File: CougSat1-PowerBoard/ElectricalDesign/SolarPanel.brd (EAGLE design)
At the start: 80 x 97 mm, 110 parts, among them J1 Wire Harness Connector, U1 SPV1040, U2 SPV1040, U3 TCA9535R, U4 LTC2499, U5 LTC2499, U6 MCP1501-18

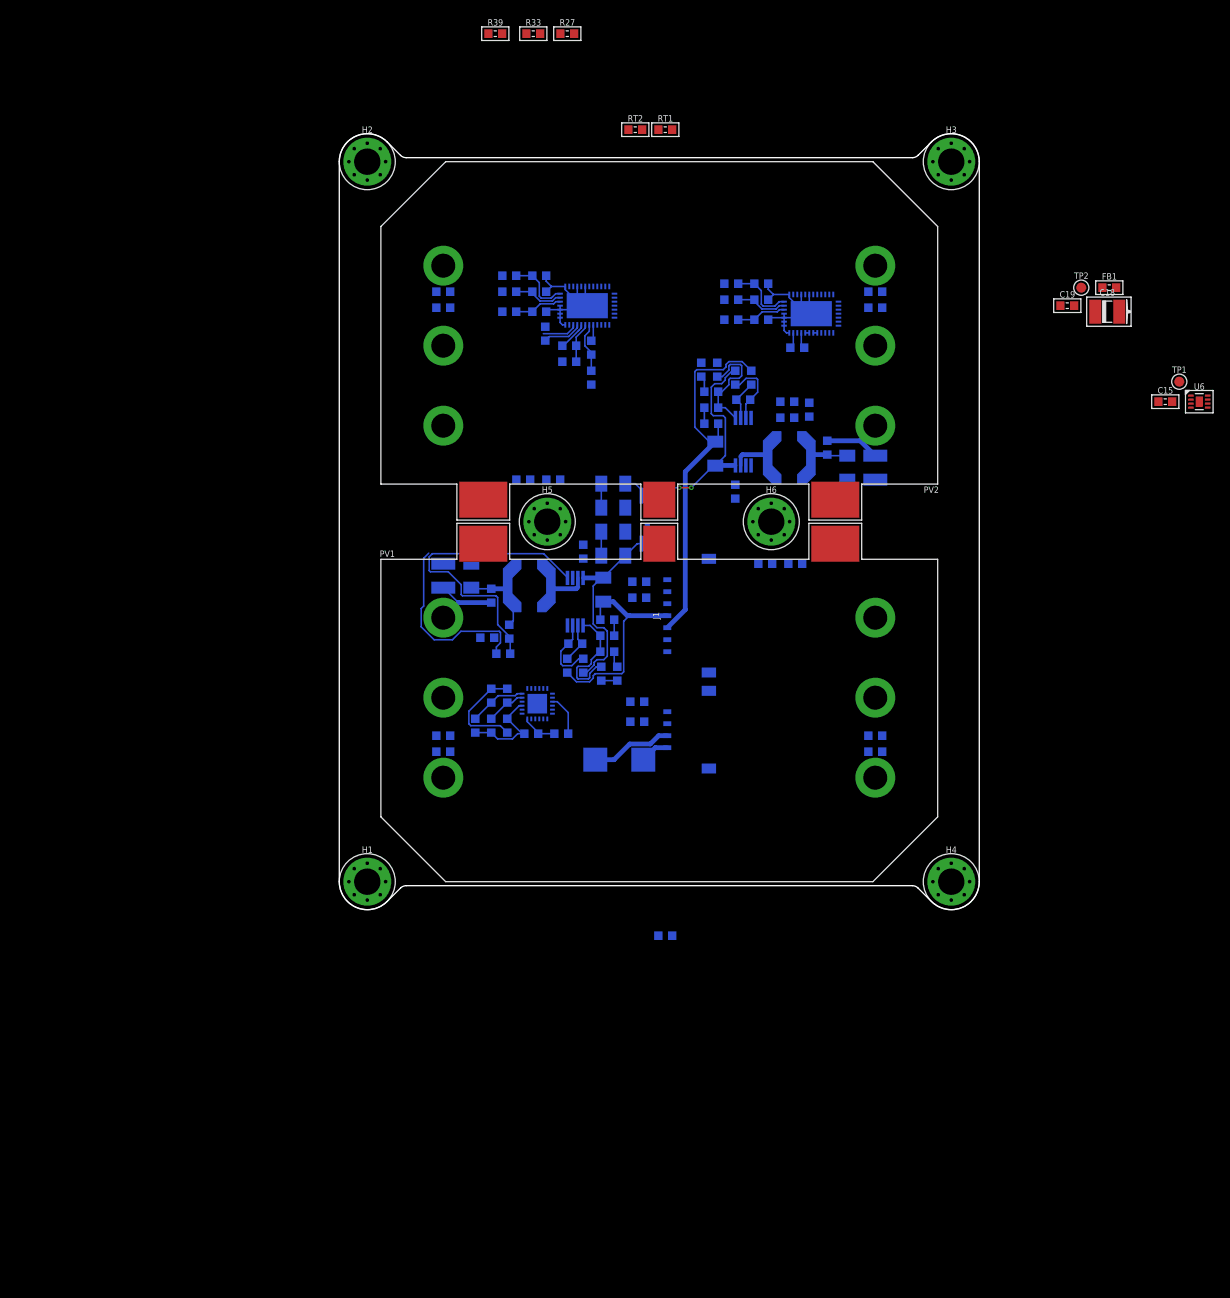
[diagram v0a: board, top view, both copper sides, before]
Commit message: Routed MPPTs, part of ADC
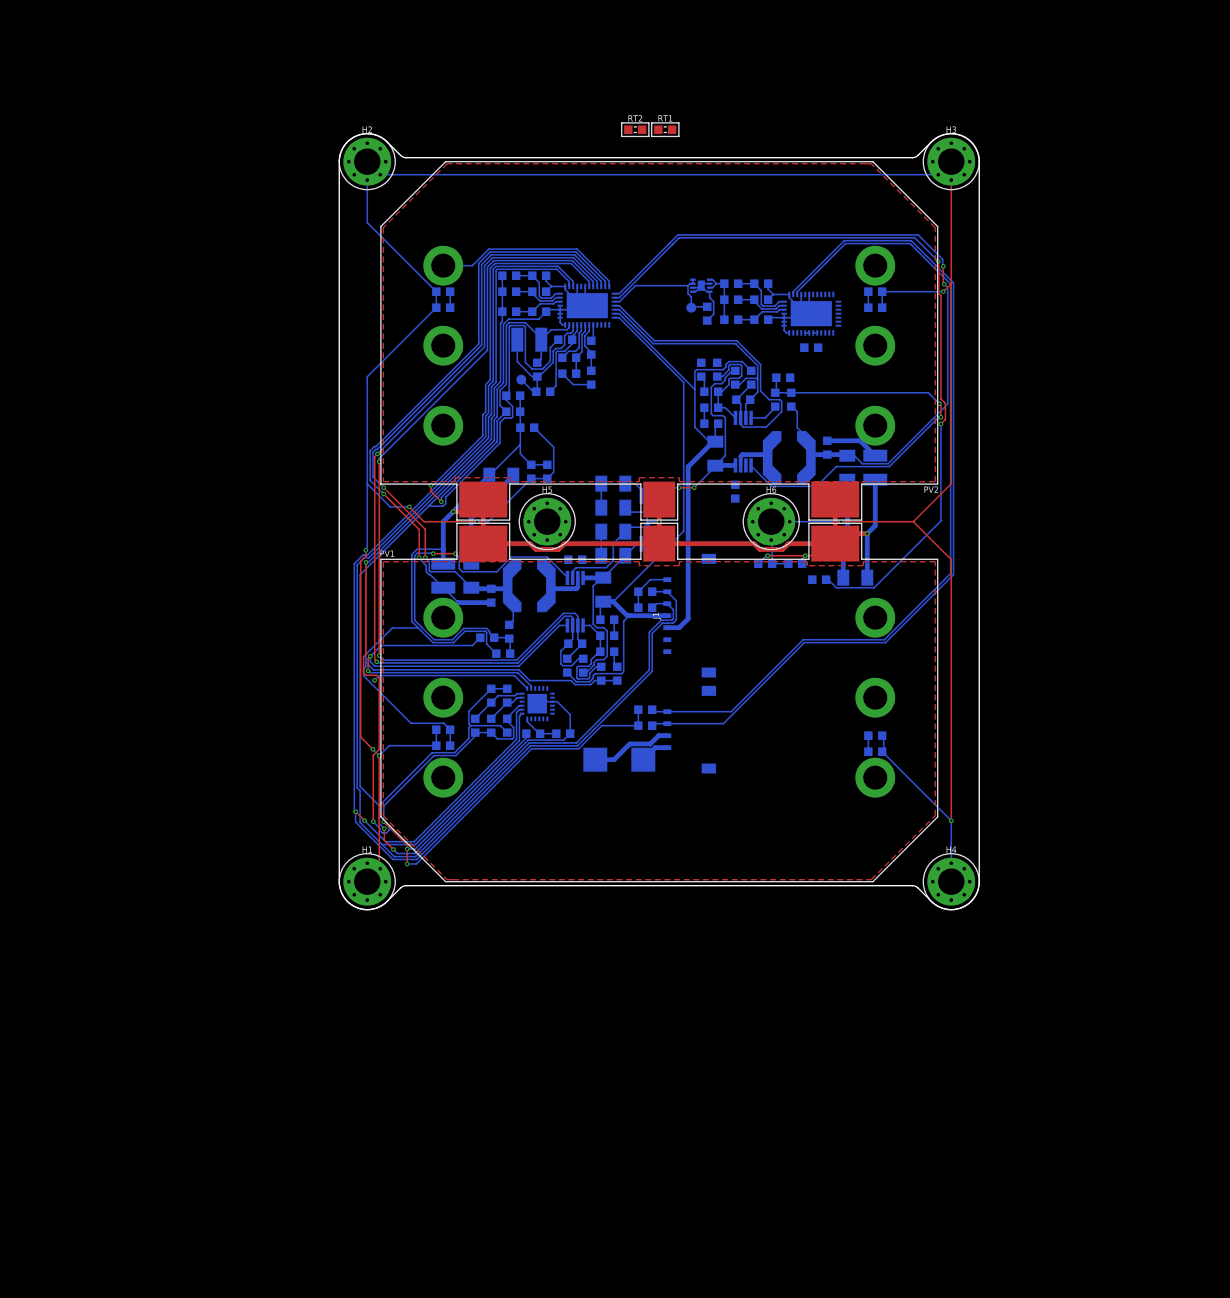
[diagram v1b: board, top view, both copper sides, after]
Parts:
- added C27, C28: 4.7µF 10%, CougsInSpace-Capacitors:3216
- moved C18 72.3 mm to (23.8, 72.2), flipped to the bottom
- moved FB1 71.9 mm to (25.5, 65.8), flipped to the bottom
- moved TP2 70.9 mm to (22.8, 67.2), flipped to the bottom
- moved C19 66.7 mm to (24.8, 68.5), flipped to the bottom, turned to 90 degrees
- moved U6 63.9 mm to (45.2, 79.0), flipped to the bottom
- moved TP1 61.7 mm to (44.0, 76.2), flipped to the bottom
- moved C15 58.3 mm to (46.0, 75.5), flipped to the bottom, turned to 270 degrees
- moved R39 49.4 mm to (23.5, 61.2), flipped to the bottom
- moved RT3 48.5 mm to (60.0, 42.2)
- moved R33 47.3 mm to (21.8, 63.2), flipped to the bottom, turned to 180 degrees
- moved R27 45.8 mm to (21.8, 65.2), flipped to the bottom, turned to 180 degrees
- moved C10 5.15 mm to (55.5, 67.5), turned to 180 degrees
- moved C17 2.61 mm to (28.2, 72.2), turned to 0 degrees
- moved R11 2.30 mm to (56.5, 64.8), turned to 270 degrees
- moved C26 1.75 mm to (59.0, 71.2), turned to 180 degrees
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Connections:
- new net OUTPUT_CAP-A: C2.2, C27.1
- new net OUTPUT_CAP-B: C28.1, C9.2
- net !MPPT_XSHUT-A: now also U3.2; no longer U3.1
- net !MPPT_XSHUT-B: now also U3.1; no longer U3.2
- net AVREF: now also U4.15; no longer U4.16
- net MPPT_ICTRL_N-A: now also U4.8; no longer U4.9
- net MPPT_ICTRL_N-B: now also U4.16; no longer U4.11
- net MPPT_ICTRL_P-A: now also U4.9; no longer U4.8
- net MPPT_ICTRL_P-B: now also U4.17; no longer U4.10
- net PGND: now also C27.2, C28.2; no longer C2.2, C9.2
- net PV_IIN_N-A: now also U4.10; no longer U4.19
- net PV_IIN_N-B: now also U4.13; no longer U4.21
- net PV_IIN_P-A: now also U4.11; no longer U4.18
- net PV_IIN_P-B: now also U4.12; no longer U4.20
- net TEMP_BACK: now also U4.14; no longer U4.17
- net TEMP_MPPT-A: now also U4.20; no longer U4.12
- net TEMP_MPPT-B: now also U4.21; no longer U4.13
- net VOUT-A: now also U4.19; no longer U4.14
- net VOUT-B: now also U4.18; no longer U4.15
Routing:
- net CHASSIS: track 108.3 -> 454.3 mm, vias 0 -> 8
- net PGND: track 25.5 -> 238.1 mm, vias 0 -> 5
- net I2C_SDA_PMIC: track 0.00 -> 182.5 mm, vias 0 -> 2
- net 3.3V: track 19.4 -> 200.2 mm, vias 0 -> 5
- net I2C_SCL_PMIC: track 0.00 -> 173.8 mm
- net DGND: track 59.1 -> 229.3 mm, vias 0 -> 2
- net I2C_SCL_ADCS: track 0.00 -> 107.2 mm
- net I2C_SDA_ADCS: track 0.00 -> 104.8 mm
- net MPPT_ICTRL_P-A: track 8.85 -> 108.3 mm, vias 0 -> 2
- net MPPT_ICTRL_N-A: track 5.35 -> 103.4 mm, vias 0 -> 2
- net AGND: track 1.48 -> 99.3 mm, vias 0 -> 2
- net TEMP_BACK: track 0.00 -> 96.1 mm, vias 0 -> 2
- net PV_IIN_N-B: track 4.77 -> 92.0 mm, vias 0 -> 2
- net PV_IIN_N-A: track 10.1 -> 80.6 mm, vias 0 -> 2
- net PV_IIN_P-A: track 9.44 -> 78.1 mm, vias 0 -> 2
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- added copper zone on layer 1, net PV_IIN_P-A
- added copper zone on layer 1, net PV_IIN_P-B

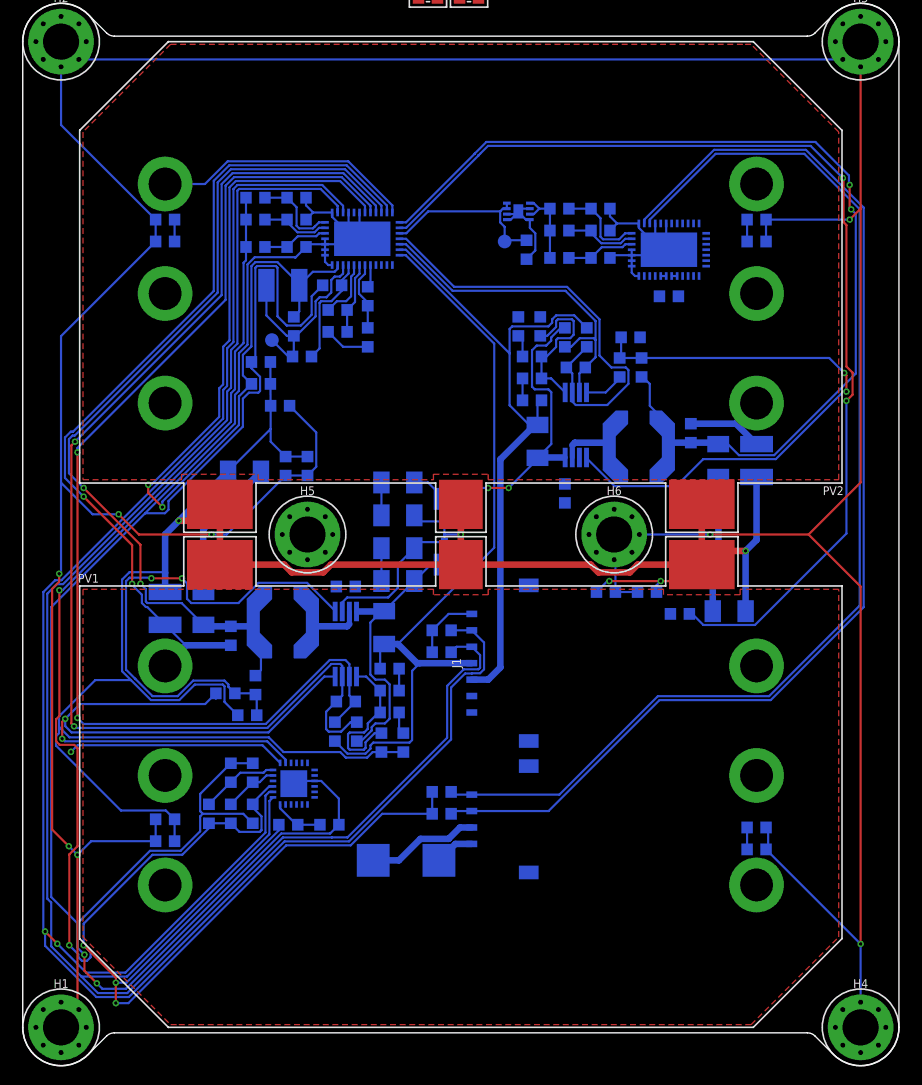
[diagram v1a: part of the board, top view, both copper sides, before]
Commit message: Routed Grounds, Power
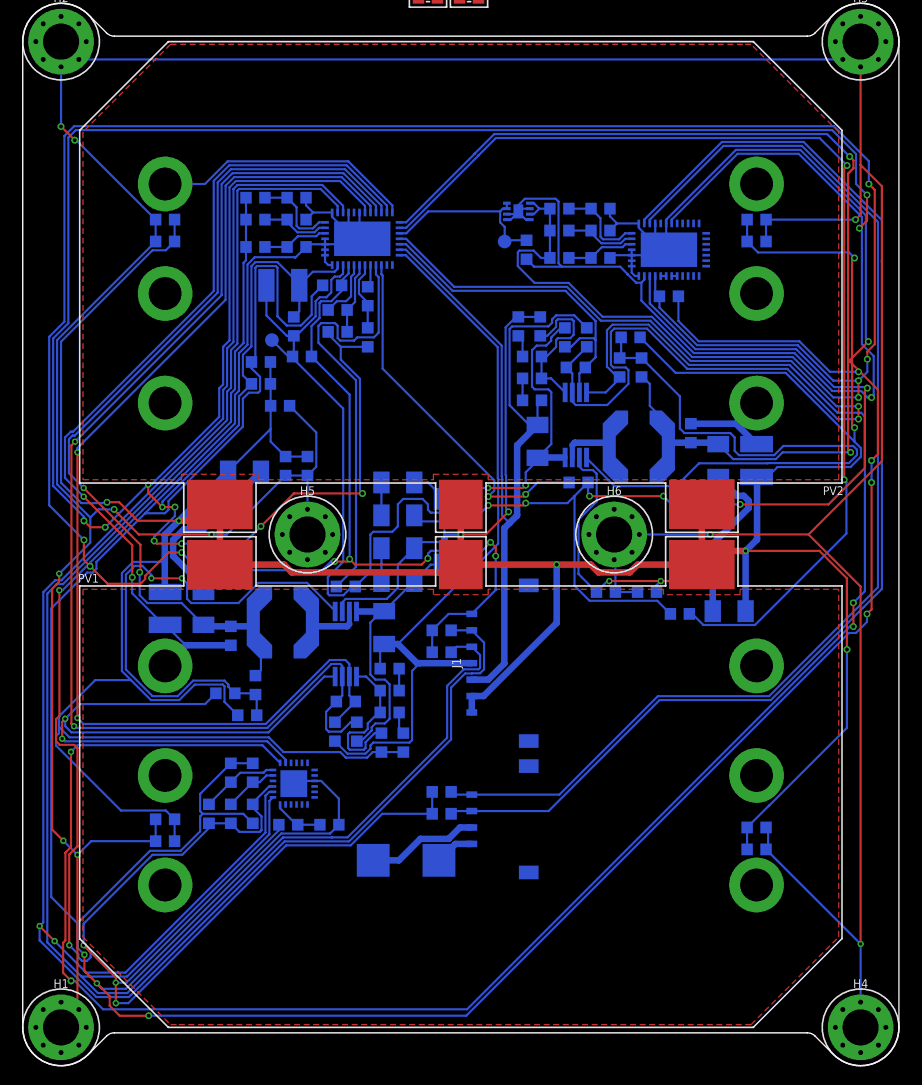
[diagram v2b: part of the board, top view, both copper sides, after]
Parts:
- moved RT4 1.60 mm to (50.8, 54.2), turned to 0 degrees
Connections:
- net TEMP_FRONT_BOTTOM: now also U4.20; no longer U4.22
- net TEMP_FRONT_TOP: now also U4.21; no longer U4.23
- net TEMP_MPPT-A: now also U4.23; no longer U4.20
- net TEMP_MPPT-B: now also U4.22; no longer U4.21
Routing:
- net 3.3V: track 200.2 -> 473.0 mm, vias 5 -> 17
- net AGND: track 99.3 -> 349.4 mm, vias 2 -> 12
- net PGND: track 238.1 -> 434.7 mm, vias 5 -> 11
- net DGND: track 229.3 -> 400.5 mm, vias 2 -> 8
- net !MPPT_XSHUT-B: track 23.7 -> 183.9 mm, vias 1 -> 4
- net AVDD: track 19.6 -> 155.5 mm, vias 0 -> 6
- net MPPT_ICTRL_N-B: track 41.1 -> 93.7 mm, vias 0 -> 2
- net TEMP_MPPT-A: track 0.00 -> 39.5 mm
- net TEMP_MPPT-B: track 0.00 -> 33.5 mm, vias 0 -> 2
- net VOUT-B: track 61.2 -> 77.2 mm
- net CHASSIS: track 454.3 -> 462.8 mm, vias 8 -> 10
- net PV_IIN_N-B: track 92.0 -> 97.9 mm
- net MPPT_SET-B: track 53.2 -> 57.7 mm, vias 2 -> 0
- net OUTPUT_CAP-A: track 13.2 -> 16.5 mm
- net OUTPUT_CAP-B: track 12.5 -> 15.1 mm
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
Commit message: Minor Routing Changes
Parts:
- moved RT3 21.8 mm to (38.2, 42.8)
- moved RT2 1.90 mm to (38.8, 97.8), flipped to the bottom, turned to 90 degrees
- moved RT1 1.25 mm to (41.8, 97.8), flipped to the bottom, turned to 90 degrees
- moved RT5 0.25 mm to (29.2, 44.8)
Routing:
- net TEMP_BACK: track 97.3 -> 125.1 mm, vias 2 -> 4
- net AVDD: track 155.5 -> 151.0 mm
- net PGND: track 434.7 -> 431.2 mm
- net CHASSIS: track 462.8 -> 465.1 mm
- net DGND: track 400.5 -> 398.8 mm
- net VOUT-A: track 70.0 -> 71.6 mm
- net 3.3V: track 473.0 -> 471.5 mm
- net AGND: track 349.4 -> 348.9 mm, vias 12 -> 11
- net I2C_SDA_ADCS: track 107.1 -> 107.6 mm
- added copper zone on layer 16, net BALANCING

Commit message: Routing Changes, Added Thermistors
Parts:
- moved RT2 97.4 mm to (9.00, 5.00), flipped to the top, turned to 180 degrees
- moved RT1 29.5 mm to (71.0, 94.0), flipped to the top, turned to 0 degrees
- moved FB1 1.00 mm to (26.5, 65.8)
- moved R27 0.75 mm to (22.5, 65.2)
- moved R33 0.75 mm to (22.5, 63.2)
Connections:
- net AVREF: now also U4.17; no longer U4.15
- net MPPT_ICTRL_N-B: now also U4.18; no longer U4.16
- net MPPT_ICTRL_P-B: now also U4.19; no longer U4.17
- net PV_IIN_N-B: now also U4.15; no longer U4.13
- net PV_IIN_P-B: now also U4.14; no longer U4.12
- net TEMP_BACK: now also U4.16; no longer U4.14
- net TEMP_FRONT_BOTTOM: now also U4.12; no longer U4.20
- net TEMP_FRONT_TOP: now also U4.13; no longer U4.21
- net VOUT-A: now also U4.21; no longer U4.19
- net VOUT-B: now also U4.20; no longer U4.18
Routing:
- net TEMP_FRONT_TOP: track 0.00 -> 178.6 mm, vias 0 -> 3
- net AVDD: track 151.0 -> 308.8 mm, vias 6 -> 11
- net TEMP_FRONT_BOTTOM: track 0.00 -> 45.9 mm, vias 0 -> 1
- net PV_IIN_P-B: track 33.4 -> 63.8 mm, vias 0 -> 1
- net PV_IIN_P-A: track 78.2 -> 86.0 mm
- net AGND: track 348.9 -> 354.8 mm
- net 3.3V: track 471.5 -> 477.2 mm, vias 17 -> 16
- net PV_IIN_N-A: track 80.7 -> 83.1 mm
- net !MPPT_XSHUT-B: track 183.7 -> 185.3 mm
- net VOUT-B: track 77.3 -> 75.8 mm
- net VOUT-A: track 71.6 -> 70.8 mm
- net DGND: track 398.8 -> 399.5 mm
